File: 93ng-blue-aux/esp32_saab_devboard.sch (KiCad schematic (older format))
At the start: 39 parts, among them J1 12V INPUT, J2 ESP32 UART, J3 USB_C_Receptacle_USB2.0, J4 Conn_02x16_Row_Letter_First, J7 I-BUS, Q1 S8050, Q2 S8050, SW1 PWR IN SELECT, U1 ESP32-WROOM-32D, U2 NCP1117-3.3_SOT223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

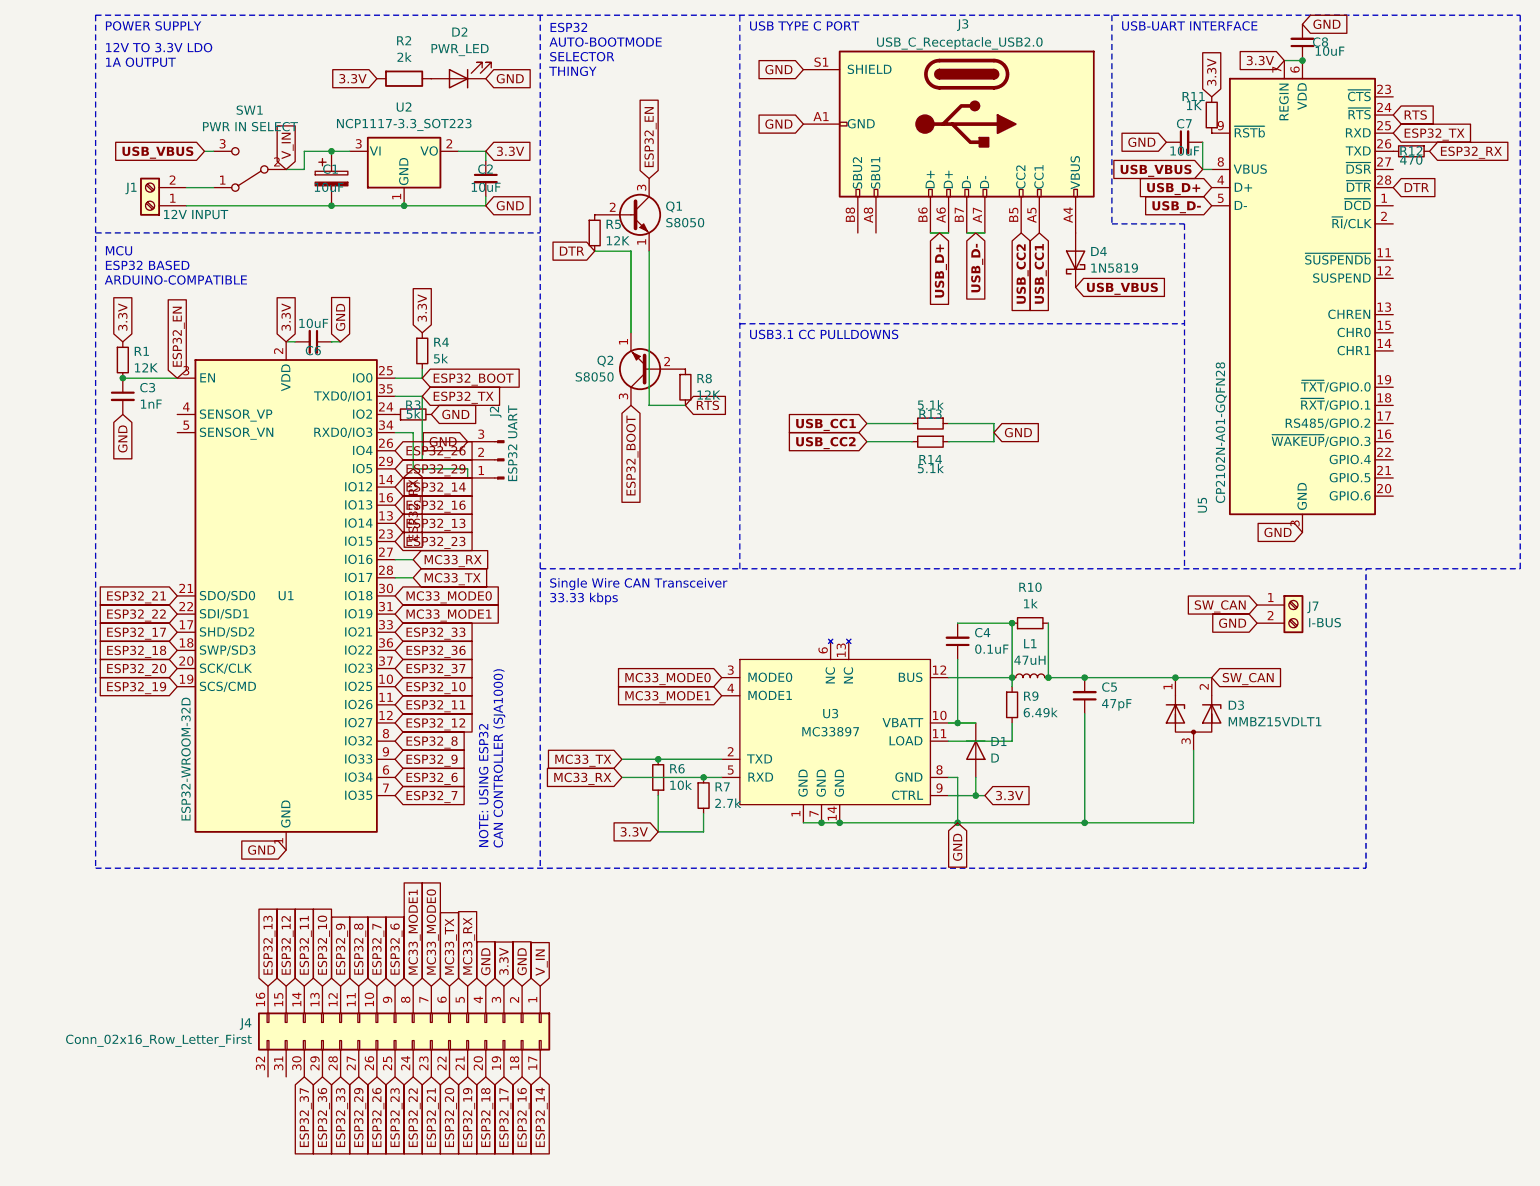
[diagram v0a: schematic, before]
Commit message: Completed first draft of final ESP32 board design, with autorouting
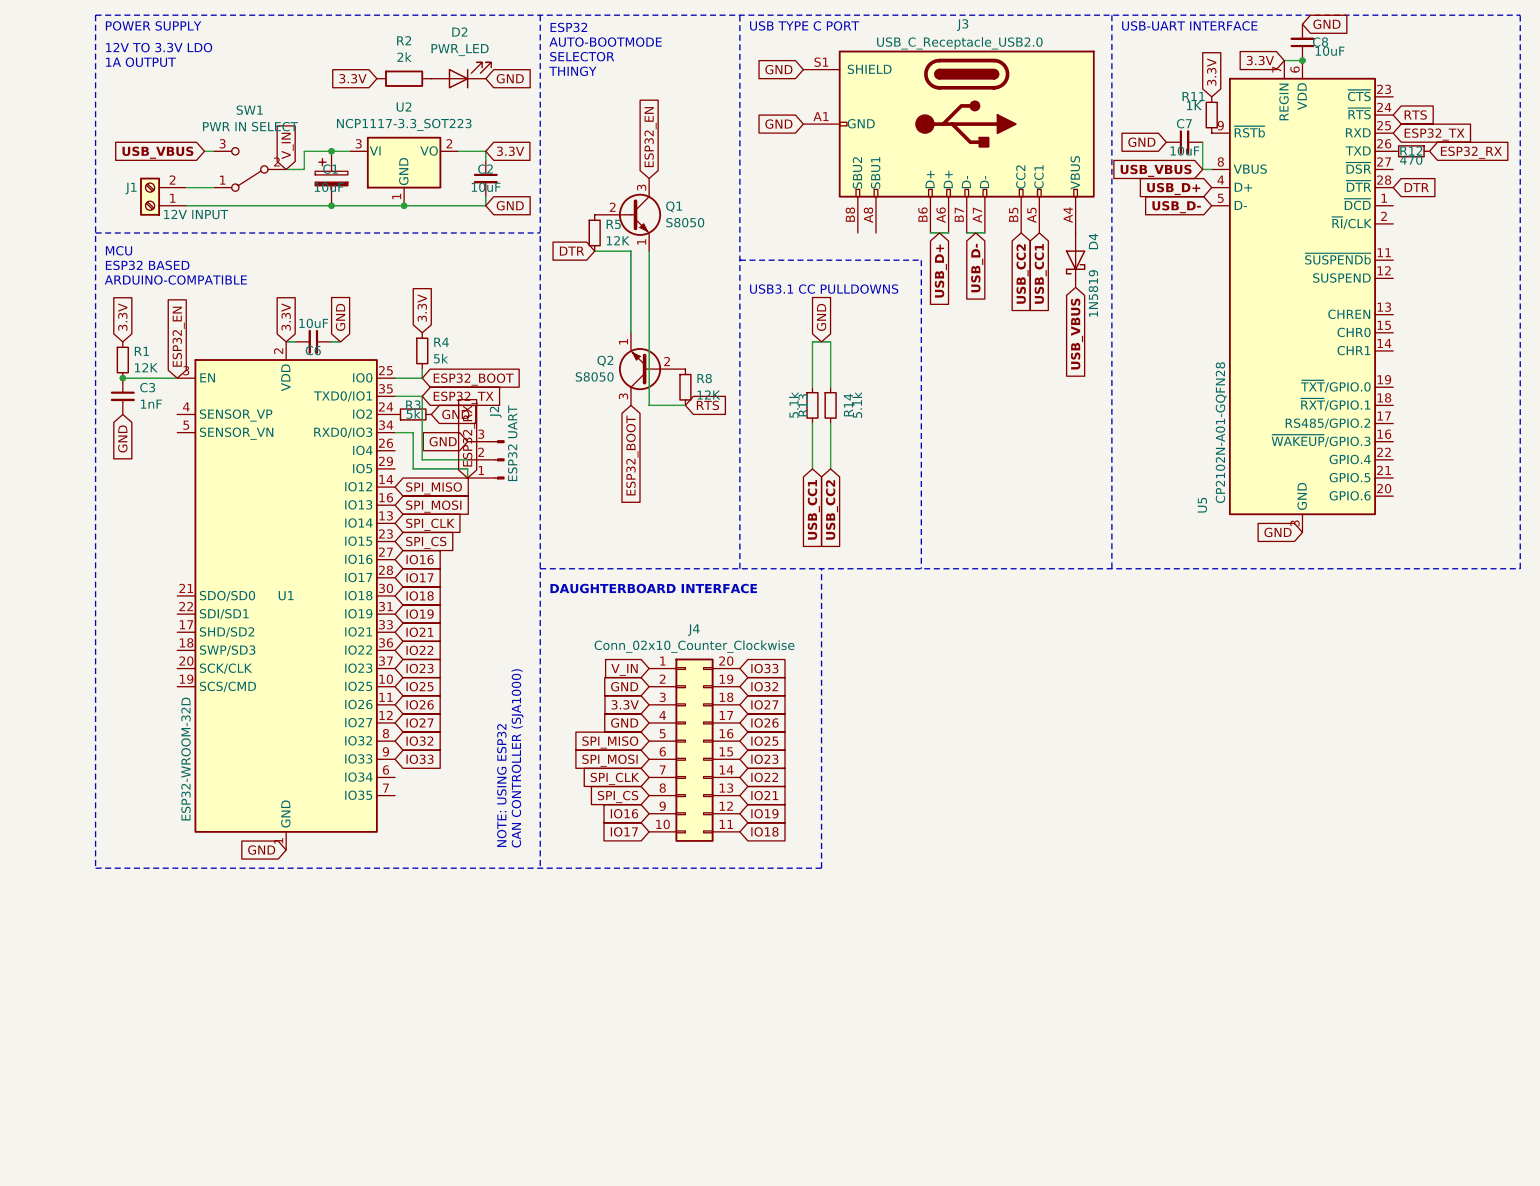
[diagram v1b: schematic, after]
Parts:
- removed C4: 0.1uF, Capacitor_SMD:C_0805_2012Metric_Pad1.15x1.40mm_HandSolder, symbol Device:C_Small
- removed C5: 47pF, Capacitor_SMD:C_0805_2012Metric_Pad1.15x1.40mm_HandSolder, symbol Device:C_Small
- removed D1: D, Diode_SMD:D_0805_2012Metric_Pad1.15x1.40mm_HandSolder, symbol Device:D
- removed D3: MMBZ15VDLT1, Package_TO_SOT_SMD:SOT-23, symbol Diode:MMBZxx
- removed J4: Conn_02x16_Row_Letter_First, Connector_PinHeader_1.00mm:PinHeader_2x16_P1.00mm_Vertical, symbol Connector_Generic:Conn_02x16_Top_Bottom
- removed J7: I-BUS, TerminalBlock_Phoenix:TerminalBlock_Phoenix_MKDS-3-2-5.08_1x02_P5.08mm_Horizontal, symbol Connector:Screw_Terminal_01x02
- removed L1: 47uH, Inductor_SMD:L_0805_2012Metric_Pad1.15x1.40mm_HandSolder, symbol Device:L_Small
- removed R10: 1k, Resistor_SMD:R_0805_2012Metric_Pad1.15x1.40mm_HandSolder, symbol Device:R_Small
- removed R6: 10k, Resistor_SMD:R_0805_2012Metric_Pad1.15x1.40mm_HandSolder, symbol Device:R_Small
- removed R7: 2.7k, Resistor_SMD:R_0805_2012Metric_Pad1.15x1.40mm_HandSolder, symbol Device:R_Small
- removed R9: 6.49k, Resistor_SMD:R_0805_2012Metric_Pad1.15x1.40mm_HandSolder, symbol Device:R_Small
- removed U3: MC33897, Package_SO:SOIC-14_3.9x8.7mm_P1.27mm, symbol custom_symbols:MC33897
- added J4: Conn_02x10_Counter_Clockwise, Connector_PinHeader_2.54mm:PinHeader_2x10_P2.54mm_Vertical, symbol Connector_Generic:Conn_02x10_Counter_Clockwise
- SW1: footprint Button_Switch_THT:SW_E-Switch_EG1271_DPDT -> Connector_PinHeader_2.54mm:PinHeader_1x03_P2.54mm_Vertical
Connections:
- net 3.3V: now also J4.3 (Pin_3)
- net GND: now also J4.2 (Pin_2), J4.4 (Pin_4)
- net V_IN: now also J4.1 (Pin_1)
- net ESP32_10 renamed IO25
- net IO25: now also J4.16 (Pin_16)
- net ESP32_11 renamed IO26
- net IO26: now also J4.17 (Pin_17)
- net ESP32_12 renamed IO27
- net IO27: now also J4.18 (Pin_18)
- net ESP32_13 renamed SPI_CLK
- net SPI_CLK: now also J4.7 (Pin_7)
- net ESP32_14 renamed SPI_MISO
- net SPI_MISO: now also J4.5 (Pin_5)
- net ESP32_16 renamed SPI_MOSI
- net SPI_MOSI: now also J4.6 (Pin_6)
- net ESP32_17: no longer names the net of U1.17 (SHD/SD2)
- net ESP32_18: no longer names the net of U1.18 (SWP/SD3)
- net ESP32_19: no longer names the net of U1.19 (SCS/CMD)
- net ESP32_20: no longer names the net of U1.20 (SCK/CLK)
- net ESP32_21: no longer names the net of U1.21 (SDO/SD0)
- net ESP32_22: no longer names the net of U1.22 (SDI/SD1)
- net ESP32_23 renamed SPI_CS
- net SPI_CS: now also J4.8 (Pin_8)
- net ESP32_26: no longer names the net of U1.26 (IO4)
- net ESP32_29: no longer names the net of U1.29 (IO5)
- net ESP32_33 renamed IO21
- net IO21: now also J4.13 (Pin_13)
- net ESP32_36 renamed IO22
- net IO22: now also J4.14 (Pin_14)
- net ESP32_37 renamed IO23
- net IO23: now also J4.15 (Pin_15)
- net ESP32_6: no longer names the net of U1.6 (IO34)
- net ESP32_7: no longer names the net of U1.7 (IO35)
- net ESP32_8 renamed IO32
- net IO32: now also J4.19 (Pin_19)
- net ESP32_9 renamed IO33
- net IO33: now also J4.20 (Pin_20)
- net MC33_MODE0 renamed IO18
- net IO18: now also J4.11 (Pin_11)
- net MC33_MODE1 renamed IO19
- net IO19: now also J4.12 (Pin_12)
- net MC33_RX renamed IO16
- net IO16: now also J4.9 (Pin_9)
- net MC33_TX renamed IO17
- net IO17: now also J4.10 (Pin_10)
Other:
- note added: "DAUGHTERBOARD INTERFACE"
- note removed: "Single Wire CAN Transceiver\n33.33 kbps"
- moved on the sheet: R13, R14

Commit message: Switched to low-profile phoenix
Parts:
- J1: footprint TerminalBlock_Phoenix:TerminalBlock_Phoenix_MKDS-3-2-5.08_1x02_P5.08mm_Horizontal -> TerminalBlock_Phoenix:TerminalBlock_Phoenix_MKDS-1,5-2-5.08_1x02_P5.08mm_Horizontal
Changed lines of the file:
@@
 F 0 "J1" H 1500 2350 50  0000 C CNN
 F 1 "12V INPUT" H 1150 2500 50  0000 C CNN
-F 2 "TerminalBlock_Phoenix:TerminalBlock_Phoenix_MKDS-3-2-5.08_1x02_P5.08mm_Horizontal" H 1400 2450 50  0001 C CNN
+F 2 "TerminalBlock_Phoenix:TerminalBlock_Phoenix_MKDS-1,5-2-5.08_1x02_P5.08mm_Horizontal" H 1400 2450 50  0001 C CNN
 F 3 "~" H 1400 2450 50  0001 C CNN
 	1    1400 2450
